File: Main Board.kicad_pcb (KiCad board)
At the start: 4 copper layers, 243.2 x 134 mm, 562 parts, among them J10 Conn_02x07_Odd_Even, J102 Speaker Out, J103 Conn_02x08_Odd_Even, J11 Conn_02x07_Odd_Even, J110 SD Holder MEM2061-01-188-00-A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, J12 Conn_02x07_Odd_Even, J13 Conn_01x03_Pin, J14 Conn_01x03_Pin, J15 Conn_01x03_Pin, J16 Conn_01x03_Pin, J17 Conn_01x03_Pin, J18 Conn_01x03_Pin, J19 Conn_01x03_Pin, J2 I2C_MAIN, J20 Conn_01x03_Pin, J21 Conn_01x03_Pin, J22 Conn_01x03_Pin, J23 Conn_01x03_Pin, J24 Conn_01x03_Pin, J25 Conn_01x03_Pin, J26 Conn_01x03_Pin, J27 Conn_01x03_Pin, J28 Conn_01x03_Pin, J29 Conn_01x03_Pin, J3 I2C_A, J30 Conn_01x03_Pin, J31 Conn_01x03_Pin, J32 Conn_01x03_Pin, J33 Conn_01x03_Pin, J34 Conn_01x03_Pin, J35 Conn_01x03_Pin, J36 Conn_01x03_Pin, J37 Conn_01x03_Pin, J38 Conn_01x03_Pin, J39 Conn_01x03_Pin, J4 I2C_B, J40 Conn_01x03_Pin, J41 Conn_01x03_Pin, J42 Conn_01x03_Pin, J43 Conn_01x03_Pin, J44 Conn_01x03_Pin, J45 VCC Select, J46 Conn_02x08_Odd_Even, J47 Conn_02x08_Odd_Even, J48 Conn_02x08_Odd_Even, J49 NEOPIXEL AUX, J5 Conn_02x07_Odd_Even, J50 RESET EN, J6 Conn_02x07_Odd_Even, J7 Conn_02x07_Odd_Even, J8 Conn_02x07_Odd_Even, J85 I2C_C, J86 I2C_D, J87 I2C_E, J88 Neopixel Header, J89 Servo Header B, J9 Conn_02x07_Odd_Even, J90 Servo Header A, J91 Servo Header C, J92 Servo Header D, J93 I2C_F, J94 I2C_G, J95 I2C_H, J96 UART_EXT, J97 Display 1, J98 Display 2, J99 VIN, P50 Conn_01x05_Pin, P51 Conn_01x07, Q1 BSS138, Q2 NPN transistor, SW1 SW_Push, SW2 SW_Push, U1 ESP32-S3-WROOM-1-N4, U10 Analog_MUX_CD4067BPWR, U11 IO_EXPANDER_TCA9535PWR, U12 IO_EXPANDER_TCA9535PWR, U13 IO_EXPANDER_TCA9535PWR, U19 Shift Register SN74HCS164PWR, U2 Analog_MUX_CD4067BPWR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

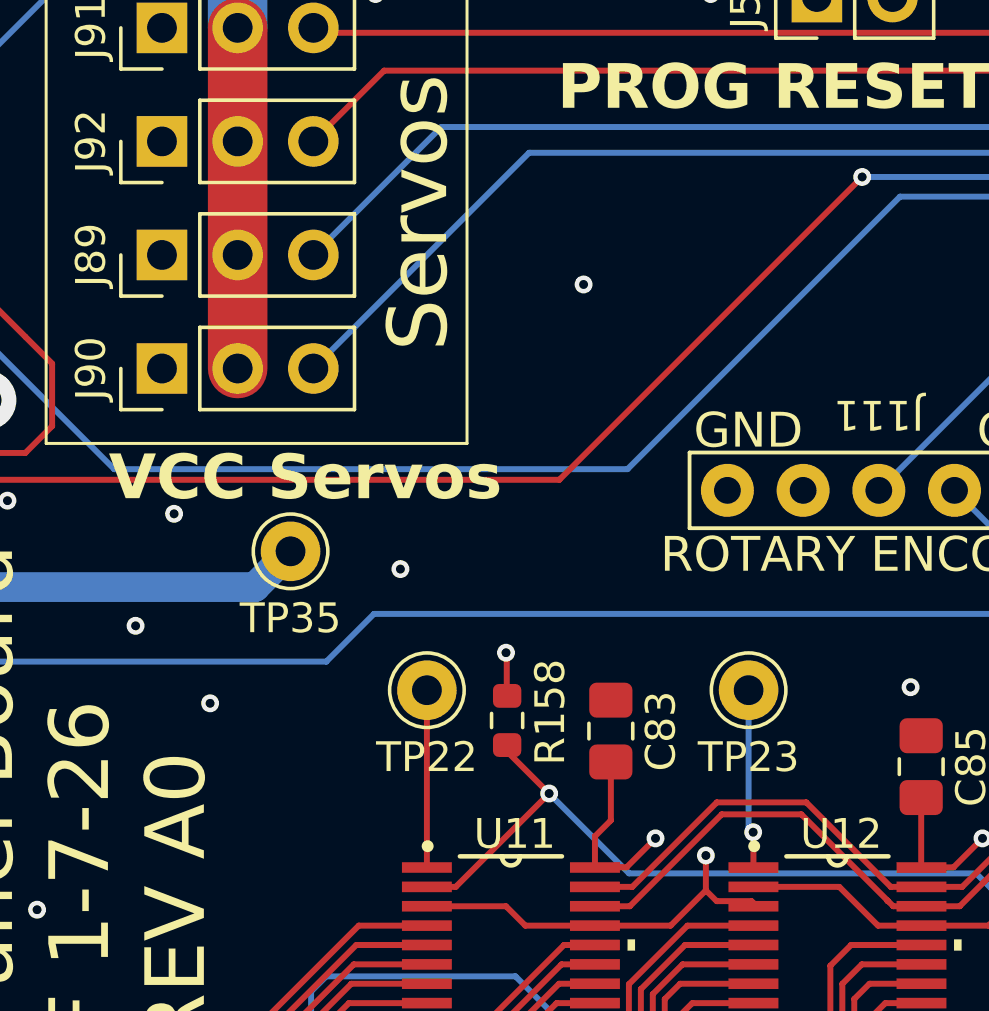
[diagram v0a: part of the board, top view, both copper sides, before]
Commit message: Added 2 test points
for possible logic level converters
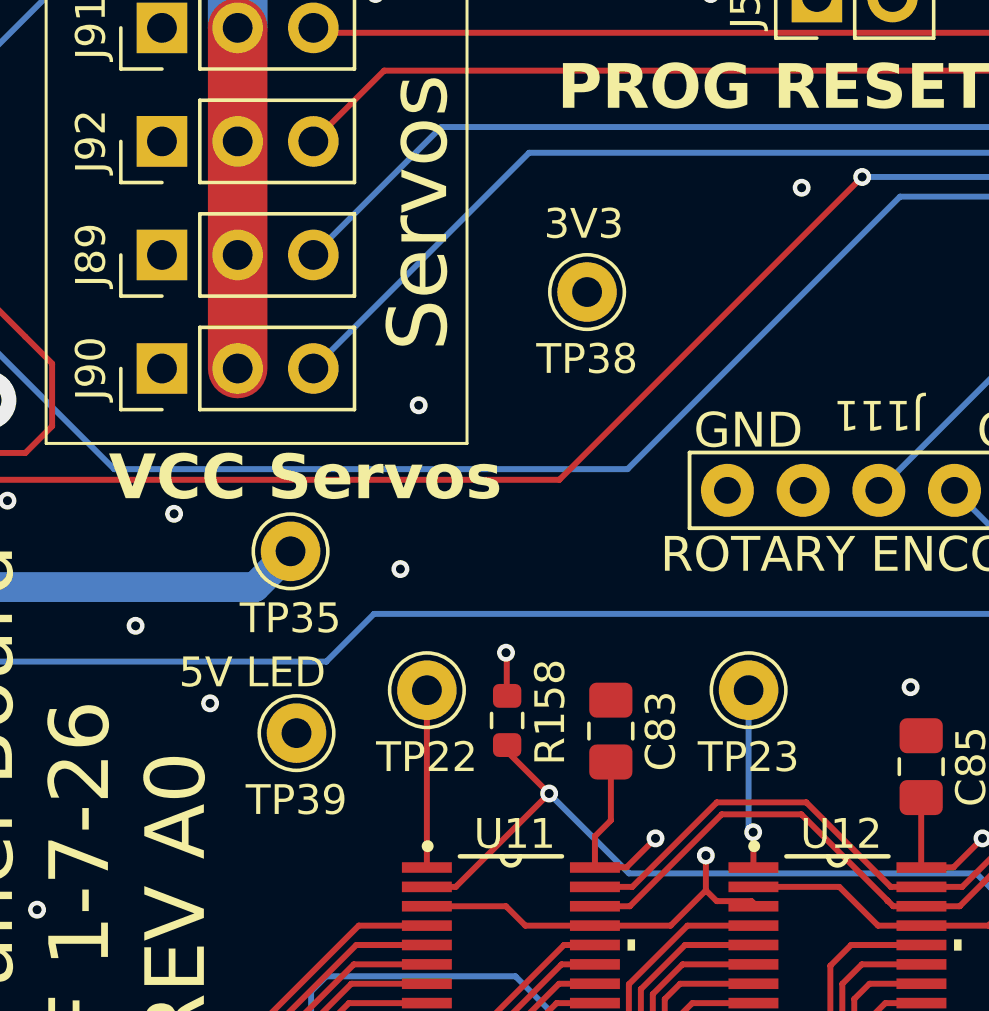
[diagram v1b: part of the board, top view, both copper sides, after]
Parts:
- added TP38: TestPoint, Connector_Pin:Pin_D1.0mm_L10.0mm, F.Cu at (160.9, 47.6)
- added TP39: TestPoint, Connector_Pin:Pin_D1.0mm_L10.0mm, F.Cu at (151.2, 62.4)
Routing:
- net GND: vias 307 -> 308
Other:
- board text added: "5V LED"
